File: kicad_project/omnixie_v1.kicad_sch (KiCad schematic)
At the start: 85 parts, among them J1 Conn_01x01, J2 Conn_01x04, J3 Conn_01x04, J4 USB_C_Receptacle_USB2.0_14P, Q0 Q_NMOS, Q1 Q_NMOS, Q10 Q_NMOS, Q100 Q_NMOS, Q11 Q_NMOS, Q2 Q_NMOS, Q3 Q_NMOS, Q4 Q_NMOS, Q5 Q_NMOS, Q6 Q_NMOS, Q7 Q_NMOS, Q8 Q_NMOS, Q9 Q_NMOS, T1 Flyback-ATB3225, U1 CH32V003F4U6, U2 4N25, U3 PI4IOE5V6416ZDEX

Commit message: component selection nearly done
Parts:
- removed D1: D, symbol Device:D
- removed H3, H4: MountingHole, MountingHole:MountingHole_2.7mm_M2.5_ISO7380_Pad_TopBottom, symbol MASTER_SYMBOLS:MountingHole_M2.5_RemoveWarning
- removed J1: Conn_01x01, symbol cnixxie:Conn_01x01
- removed N2, N3, N4, N5, N6: IN-1, NIXIE:IN-1_NIXIE_v1, symbol nixies-us:IN-1
- removed N9: IN-3, nixies-us:nixies-us-IN-3, symbol nixies-us:IN-3
- removed NX2, NX3, NX4, NX5, NX6: IN-12BORIGINAL, NIXIE:IN-12A Nixie, symbol nixies-us:IN-12BORIGINAL
- removed Q100: Q_NMOS, symbol Transistor_FET:Q_NMOS_GSD
- removed R10, R3, R5, R7, R? (x2): R, symbol cnixxie:R
- removed T1: Flyback-ATB3225, Flyback-ATB3225:Flyback-ATB3225, symbol cnixxie:Flyback-ATB3225
- removed TP1: VINPUT, symbol Connector:TestPoint
- removed TP2: VD, symbol Connector:TestPoint
- removed TP3: VOUTPUT, symbol Connector:TestPoint
- removed TP4: VFB, symbol Connector:TestPoint
- removed TP5: GATE, symbol Connector:TestPoint
- removed TP?: IOUTSENSE, symbol Connector:TestPoint
- removed TP?: IINSENSE, symbol Connector:TestPoint
- removed U2: 4N25, Package_DIP:DIP-6_W7.62mm, symbol Isolator:4N25
- added C3, C4, C5: 1uF, Capacitor_SMD:C_0805_2012Metric, symbol Device:C
- added FID5, FID6, FID7, FID8: Fiducial, Fiducial:Fiducial_0.5mm_Mask1mm, symbol MASTER_SYMBOLS:Fiducial
- added J1, J5: Conn_01x04, Connector_PinHeader_2.54mm:PinHeader_1x04_P2.54mm_Vertical, symbol Connector_Generic:Conn_01x04
- added J6, J7: Conn_01x02, Connector_PinHeader_2.54mm:PinHeader_1x02_P2.54mm_Vertical, symbol Connector_Generic:Conn_01x02
- C1: value C -> 10uF; footprint (none) -> Capacitor_SMD:C_0805_2012Metric
- C2: renamed from C?; value C -> 0.22uF; footprint (none) -> Capacitor_SMD:C_1210_3225Metric
- D2: renamed from D?; value D -> SK3200AFL-TP; footprint (none) -> OMNIXIE:SK3200AFL
- H1, H2: footprint MountingHole:MountingHole_2.7mm_M2.5_ISO7380_Pad_TopBottom -> MountingHole:MountingHole_2.2mm_M2_DIN965_Pad_TopOnly
- J2, J3: value Conn_01x04 -> SM04B-SRSS-TB
- J4: value USB_C_Receptacle_USB2.0_14P -> USB4105-GF-A
- N1, R1, R2: now not fitted; now left out of the parts list
- N2: renamed from NX1; now not fitted; now left out of the parts list
- N7, N8: value IN-3 -> IN-3/DOT; now not fitted; now left out of the parts list
- Q0, Q1, Q10, Q11, Q2, Q3, Q4, Q5, Q6, Q7, Q8, Q9: value Q_NMOS -> BSS123
- Q12: renamed from Q?; value Q_NMOS -> IPN50R1K4CEATMA1; footprint (none) -> Package_TO_SOT_SMD:SOT-223-3_TabPin2
- R11, R12: renamed from R?; value R -> 1k; footprint (none) -> Resistor_SMD:R_0805_2012Metric
- R13, R14: renamed from R?; footprint (none) -> Resistor_SMD:R_0603_1608Metric
- R15: renamed from R?; footprint (none) -> Resistor_SMD:R_0402_1005Metric_Pad0.72x0.64mm_HandSolder
- R3, R5: renamed from R?; value R -> 4.42m; footprint (none) -> Resistor_SMD:R_0402_1005Metric_Pad0.72x0.64mm_HandSolder
- R4: value R -> 82k; now not fitted; now left out of the parts list
- R6: value R -> 15k; footprint (none) -> Resistor_SMD:R_2010_5025Metric
- R7: renamed from R?; value R -> 100k; footprint (none) -> Resistor_SMD:R_0805_2012Metric
- R8, R9: value R -> 47; footprint (none) -> Resistor_SMD:R_0402_1005Metric_Pad0.72x0.64mm_HandSolder
- T2: renamed from T?; value Flyback-ATB3225 -> ATB322515-0110; footprint Flyback-ATB3225:Flyback-ATB3225 -> OMNIXIE:ATB322515
- TP10: renamed from TP?; value VINPUT -> 5005; footprint (none) -> TestPoint:TestPoint_Keystone_5005-5009_Compact
- TP11: renamed from TP?; value VD -> 5005; footprint (none) -> TestPoint:TestPoint_Keystone_5005-5009_Compact
- TP12: renamed from TP?; value VOUTPUT -> 5005; footprint (none) -> TestPoint:TestPoint_Keystone_5005-5009_Compact
- TP13: renamed from TP?; value VFB -> 5005; footprint (none) -> TestPoint:TestPoint_Keystone_5005-5009_Compact
- TP14: renamed from TP?; value GATE -> 5005; footprint (none) -> TestPoint:TestPoint_Keystone_5005-5009_Compact
- TP6: renamed from TP?; value IINSENSE -> 5005; footprint (none) -> TestPoint:TestPoint_Keystone_5005-5009_Compact
- TP8: renamed from TP?; value IOUTSENSE -> 5005; footprint (none) -> TestPoint:TestPoint_Keystone_5005-5009_Compact
- gave numbers to parts that had none: 1
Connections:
- net FEEDBACK is gone; now on net HV_FEEDBACK: R11.1, R7.2, TP13.1
- net INT_GATE is gone; now on net HV_SW: Q12.1 (G), R12.1, TP14.1
- net +3V3: now also C3.1, J1.3 (Pin_3), J5.3 (Pin_3)
- net +5V: now also C1.1, R3.2, TP10.1, C4.1, C5.1, J6.1 (Pin_1), J7.1 (Pin_1); no longer R3.1, T2.1, TP6.1
- net CATHAUX: now also N8.K
- net D+: now also R9.1; no longer U1.17 (PD3/A4/T2CH2/AETR/UCTS/T1CH4)
- net D-: now also R8.1; no longer R15.1, U1.18 (PD4/A7/UCK/T2CH1ETR/OPO/T1CH4ETR)
- net DPU: now also R15.1; no longer R15.2
- net GND: now also C3.2, C4.2, C5.2, J1.4 (Pin_4), J5.4 (Pin_4), J6.2 (Pin_2), J7.2 (Pin_2); no longer R9.2
- net HIGHVOLTAGE: now also R4.2; no longer R4.1, R5.1, R7.1, TP12.1
- net I2C_SCL: now also J1.2 (Pin_2), J5.2 (Pin_2)
- net I2C_SDA: now also J1.1 (Pin_1), J5.1 (Pin_1)
- net at N7.A: now also R4.1
- net at N7.K: now also N8.A
- net HV_FEEDBACK: now reaches U1.11 (PC4/A2/T1CH4/MCO/T1CH1CH2N)
- net HV_SW: now reaches U1.2 (PA1/OSCI/A1/T1CH2/OPN0)
- net at R6.2: now also R5.1, R7.1, TP12.1
- net at R8.2: now also R15.2, U1.18 (PD4/A7/UCK/T2CH1ETR/OPO/T1CH4ETR); no longer R9.1
- net IOUTSENSE: no longer names the net of C2.1, D2.1 (K), R5.2, TP8.1
- new net: R3.1, T2.1, TP6.1
- new net: R9.2, U1.17 (PD3/A4/T2CH2/AETR/UCTS/T1CH4)
- no-connect marks 0 -> 10
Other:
- note added: "+3V3 LDO"
- note added: "+5V Output"
- note added: "1:10 Turns Ratio"
- note added: "2 options for nixie hat connector"
- note added: "2.54mm Header Connections"
- note added: "Add PNs to BOM (saved in OneTab)"
- note added: "Compatibility for Driving the IN3s and the other small bulb looking ones"
- note added: "Figure out pinout for USB and analog inputs"
- note added: "Find small bulb sockets for the small nixie bulbs"
- note added: "Footprints for remaining components"
- note added: "For Driving Cathode MOSFETs"
- note added: "High Voltage! Flyback!"
- note added: "I/O Expander"
- note added: "I2C via..."
- note added: "It would be nice if the connector that connects the driver supply board to the nixie was reasonable to source"
- note added: "MOSFET Cathode Drivers"
- note added: "Maybe buy both and layout both connectors???"
- note added: "OMNIXIE"
- note added: "Output to Nixie Hat"
- note added: "QWIIC Compatible Connectors"
- note added: "Remaining passives values"
- note added: "Supply Input"
- note added: "The nixie driver supply board (Omnixie) would be awesome if all you had to do was either fab a super simple board or etch and homemake a nixie daughter board to use"
- note added: "To-Do"
- note added: "USB Compatibility"
- note added: "Vertical USB-C footprint"
- note added: "or"
- note removed: "Also I need to find a 200 V tolerant connector anyways if I'm going with the I2C GPIO approach anywas I require a connector that is at least 5 pins and relatively easy to take apart"
- note removed: "For control internally"
- note removed: "For dev and experimentation"
- note removed: "Unless I can find a relatively non-unicorn ~200V tolerant connector that has 12 pins, the mosfets will be on the nixie footprint board"
- company: (none) -> High Tech Aztech
- title: (none) -> Omnixie
- moved on the sheet: C2, D2, FID1, FID2, FID3, FID4, H1, H2, J2, J3, J4, Q0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

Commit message: component placement commencing
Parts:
- added J8: IL-WX-16S-VF-B-E1000E, OMNIXIE:IL-WX-16S-VF-B-E1000E-SOCKET, symbol Connector_Generic:Conn_02x08_Counter_Clockwise
- FID1, FID2, FID3, FID4, FID5, FID6, FID7, FID8: now not fitted
- H1, H2: footprint MountingHole:MountingHole_2.2mm_M2_DIN965_Pad_TopOnly -> MountingHole:MountingHole_2.2mm_M2
- J4: footprint Connector_USB:USB_C_Receptacle_Palconn_UTC16-G -> OMNIXIE:USB4120-03-C
- renumbered D2 to D1, T2 to T1
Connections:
- net CATH0: now also J8.1 (Pin_1)
- net CATH1: now also J8.2 (Pin_2)
- net CATH2: now also J8.3 (Pin_3)
- net CATH3: now also J8.4 (Pin_4)
- net CATH4: now also J8.5 (Pin_5)
- net CATH5: now also J8.6 (Pin_6)
- net CATH6: now also J8.7 (Pin_7)
- net CATH7: now also J8.8 (Pin_8)
- net CATH8: now also J8.9 (Pin_9)
- net CATH9: now also J8.10 (Pin_10)
- net CATHAUX: now also J8.12 (Pin_12)
- net CATHDP: now also J8.11 (Pin_11)
- net D+: now also R9.2, U1.17 (PD3/A4/T2CH2/AETR/UCTS/T1CH4)
- net D-: now also R15.2, R8.2, U1.18 (PD4/A7/UCK/T2CH1ETR/OPO/T1CH4ETR)
- net HIGHVOLTAGE: now also J8.15 (Pin_15), J8.16 (Pin_16)
- net at R3.1, T1.1, TP6.1: no longer names the net of R3.1, T1.1, TP6.1
- net HV_1: now reaches R5.1, R6.2, R7.1, TP12.1
- net D_2: now reaches C2.1, D1.1 (K), R5.2, TP8.1
- net D_1: now reaches D1.2 (A), T1.3, TP11.1
- net CC1: now reaches J4.A5 (CC1), R13.1
- net CC2: now reaches J4.B5 (CC2), R14.2
- no-connect marks 10 -> 12
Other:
- note added: "Done"
- note added: "Each board is individually programmed with the same program and communicate via I2C with each other to determine what each digit is"
- note added: "Idea"
- note added: "Next Revision?"
- note added: "PROGRAM pinout to edge?"
- note added: "Pinout of connector that could work well for routing nixie hat footprint"
- note added: "The connector that connects both boards should be reasonably sourceable"
- note added: "The nixie driver supply board will be separate from the nixie hat"
- note added: "change 1uf 1k and 100k to lower package size"
- note removed: "2 options for nixie hat connector"
- note removed: "It would be nice if the connector that connects the driver supply board to the nixie was reasonable to source"
- note removed: "Maybe buy both and layout both connectors???"
- note removed: "This means the power supplying must occur not on the nixie footprint board, but on the driver board"
- moved on the sheet: H1, H2, R13, R14

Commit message: more component placement
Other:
- note added: "Likely remove pinout on the right side of board"
- note added: "add diff pair to stackup, calculate width and spacing using calculator. standard FR4"
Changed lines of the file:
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@@
 		)
 	)
+	(text "add diff pair to stackup, calculate width and spacing using calculator. standard FR4"
+		(exclude_from_sim no)
+		(at 16.51 272.796 0)
+		(effects
+			(font
+				(size 1.27 1.27)
+				(thickness 0.3556)
+				(bold yes)
+				(italic yes)
+			)
+			(justify left)
+		)
+	)
 	(text "Vertical USB-C footprint\n"
 		(exclude_from_sim no)
@@
 		)
 	)
+	(text "Likely remove pinout on the right side of board"
+		(exclude_from_sim no)
+		(at 46.482 266.7 0)
+		(effects
+			(font
+				(size 1.27 1.27)
+				(thickness 0.3556)
+				(bold yes)
+				(italic yes)
+			)
+			(justify left)
+		)
+	)
 	(text "Output to Nixie Hat"
 		(exclude_from_sim no)
@@
 	(wire
 		(pts
-			(xy 63.5 152.4) (xy 66.04 152.4)
-		)
-		(stroke
-			(width 0)
-			(type default)
-		)
-	)
-	(wire
-		(pts
 			(xy 276.86 40.64) (xy 279.4 40.64)
 		)
@@
 	(symbol
 		(lib_id "power:+5V")
-		(at 63.5 152.4 0)
+		(at 66.04 152.4 0)
 		(unit 1)
 		(exclude_from_sim no)
@@
 		(dnp no)
 		(property "Reference" "#PWR033"
-			(at 63.5 156.21 0)
+			(at 66.04 156.21 0)
 			(effects
 				(font
@@
 		)
 		(property "Value" "+5V"
-			(at 62.992 147.828 0)
+			(at 65.532 147.828 0)
 			(effects
 				(font
@@
 		)
 		(property "Footprint" ""
-			(at 63.5 152.4 0)
+			(at 66.04 152.4 0)
 			(effects
 				(font
@@
 		)
 		(property "Datasheet" ""
-			(at 63.5 152.4 0)
+			(at 66.04 152.4 0)
 			(effects
 				(font
@@
 		)
 		(property "Description" "Power symbol creates a global label with name \"+5V\""
-			(at 63.5 152.4 0)
+			(at 66.04 152.4 0)
 			(effects
 				(font

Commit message: reworking the board. Its a prototype not production ready
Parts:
- removed H1, H2: MountingHole, MountingHole:MountingHole_2.2mm_M2, symbol MASTER_SYMBOLS:MountingHole_M2.5_RemoveWarning
- removed J1: Conn_01x04, Connector_PinHeader_2.54mm:PinHeader_1x04_P2.54mm_Vertical, symbol Connector_Generic:Conn_01x04
- removed J7: Conn_01x02, Connector_PinHeader_2.54mm:PinHeader_1x02_P2.54mm_Vertical, symbol Connector_Generic:Conn_01x02
- added D2, D8: GREEN, LED_SMD:LED_0603_1608Metric, symbol MASTER_SYMBOLS:LED_Small
- added FID10, FID11, FID12, FID13, FID14, FID15, FID9: Fiducial, Fiducial:Fiducial_0.5mm_Mask1mm, symbol MASTER_SYMBOLS:Fiducial
- added J1: Conn_01x10, Connector_PinHeader_2.54mm:PinHeader_1x10_P2.54mm_Vertical, symbol Connector_Generic:Conn_01x10
- added JP10: Jumper_2_Bridged, MASTER_FOOTPRINTS:SolderJumper_Rect_0.2mm_spacing, symbol Jumper:Jumper_2_Bridged
- added JP11: Jumper_2_Bridged, MASTER_FOOTPRINTS:SolderJumper_Circular_0.2mm_spacing, symbol Jumper:Jumper_2_Bridged
- added JP12: Jumper_2_Bridged, MASTER_FOOTPRINTS:SolderJumper_Circular_0.1mm_spacing, symbol Jumper:Jumper_2_Bridged
- added JP13: Jumper_2_Bridged, MASTER_FOOTPRINTS:SolderJumper_PinHeader_0.1mm_spacing, symbol Jumper:Jumper_2_Bridged
- added JP14: Jumper_2_Bridged, MASTER_FOOTPRINTS:SolderJumper_Circular_0.05mm_spacing, symbol Jumper:Jumper_2_Bridged
- added JP4: SMT_THERM_JMP, Jumper:SolderJumper-2_P1.3mm_Bridged_RoundedPad1.0x1.5mm, symbol MASTER_SYMBOLS:SolderJumper_2_Bridged_4
- added JP5: TH_THERM_JMP, Jumper:SolderJumper-2_P1.3mm_Open_RoundedPad1.0x1.5mm, symbol MASTER_SYMBOLS:SolderJumper_2_Open
- added JP7: Jumper_2_Bridged, MASTER_FOOTPRINTS:SolderJumper_Rect_0.3mm_spacing, symbol Jumper:Jumper_2_Bridged
- added R10, R16: 10k, Resistor_SMD:R_0402_1005Metric, symbol MASTER_SYMBOLS:R_Small_17
- C3, C4, C5: footprint Capacitor_SMD:C_0805_2012Metric -> Capacitor_SMD:C_0603_1608Metric
- J6: footprint Connector_PinHeader_2.54mm:PinHeader_1x02_P2.54mm_Vertical -> Connector_PinHeader_2.54mm:PinHeader_1x03_P2.54mm_Vertical; symbol Connector_Generic:Conn_01x02 -> Connector_Generic:Conn_01x03
- R11, R12: footprint Resistor_SMD:R_0805_2012Metric -> Resistor_SMD:R_0603_1608Metric
- R3, R5: value 4.42m -> 10m; footprint Resistor_SMD:R_0402_1005Metric_Pad0.72x0.64mm_HandSolder -> Resistor_SMD:R_0603_1608Metric
- R7: footprint Resistor_SMD:R_0805_2012Metric -> Resistor_SMD:R_0402_1005Metric_Pad0.72x0.64mm_HandSolder
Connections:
- net +3V3: now also D8.2 (A), JP4.1 (A); no longer U3.21 (VDD_P), U3.23 (VDD_I2C)
- net +5V: now also D2.2 (A), JP5.1 (A); no longer C5.1, R3.2, T1.2, TP10.1
- net D+: no longer R9.2, U1.17 (PD3/A4/T2CH2/AETR/UCTS/T1CH4)
- net D-: no longer R15.2, R8.2, U1.18 (PD4/A7/UCK/T2CH1ETR/OPO/T1CH4ETR)
- net DIG_0: now also U3.2 (IO0_1); no longer U3.1 (IO0_0)
- net DIG_1: now also U3.1 (IO0_0); no longer U3.2 (IO0_1)
- net DIG_2: now also U3.4 (IO0_3); no longer U3.3 (IO0_2)
- net DIG_3: now also U3.3 (IO0_2); no longer U3.4 (IO0_3)
- net DIG_4: now also U3.6 (IO0_5); no longer U3.5 (IO0_4)
- net DIG_5: now also U3.5 (IO0_4); no longer U3.6 (IO0_5)
- net DIG_6: now also U3.8 (IO0_7); no longer U3.7 (IO0_6)
- net DIG_7: now also U3.7 (IO0_6); no longer U3.8 (IO0_7)
- net DIG_8: now also U3.11 (IO1_1); no longer U3.10 (IO1_0)
- net DIG_9: now also U3.10 (IO1_0); no longer U3.11 (IO1_1)
- net DIG_AUX: now also U3.12 (IO1_2); no longer U3.13 (IO1_3)
- net DIG_DP: now also U3.13 (IO1_3); no longer U3.12 (IO1_2)
- net GND: now also R10.1, R16.1
- net HV_SW: now also U1.14 (PC7/MISO/T1CH2/T2CH2/URTS); no longer U1.2 (PA1/OSCI/A1/T1CH2/OPN0)
- net I2C_SCL: now also J5.1 (Pin_1); no longer J5.2 (Pin_2)
- net I2C_SDA: now also J5.2 (Pin_2); no longer J5.1 (Pin_1)
- net PROGRAM: now also J6.3 (Pin_3)
- net PD7: now reaches U1.1 (PD7/NRST/T2CH4/OPP1/UCK)
- net PD7: now also J1.9 (Pin_9)
- net PC5: now reaches U1.12 (PC5/SCK/T1ETR/T2CH1ETR/SCL/UCK/T1CH3)
- net PC5: now also J1.3 (Pin_3)
- net PC6: now reaches U1.13 (PC6/MOSI/T1CH1CH3/UCTS/SDA)
- net PC6: now also J1.2 (Pin_2)
- net PD2: now reaches U1.16 (PD2/A3/T1CH1/T2CH3/T1CH2N)
- net PD2: now also J1.1 (Pin_1)
- net PD6: now reaches U1.20 (PD6/A7/URX/T2CH3/UTX)
- net PD6: now also J1.10 (Pin_10)
- net PA2: now reaches U1.3 (PA2/OSCO/A0/T1CH2N/OPP0/AETR2)
- net PA2: now also J1.7 (Pin_7)
- net PD0: now reaches U1.5 (PD0/T1CH1N/OPN1/SDA/UTX)
- net PD0: now also J1.6 (Pin_6)
- net PC0: now reaches U1.7 (PC0/T2CH3/UTX/NSS/T1CH3)
- net PC0: now also J1.5 (Pin_5)
- net PC1: now reaches U1.8 (PC1/SDA/NSS/T2CH4/T2CH1ETR/T1BKIN/URX)
- net PC1: now also J1.4 (Pin_4)
- new net: JP4.2 (B), U3.21 (VDD_P), U3.23 (VDD_I2C)
- new net: D2.1 (K), R16.2
- new net: D8.1 (K), R10.2
- new net +5V_FLY: C5.1, JP5.2 (B), R3.2, T1.2, TP10.1
- new net D+_1: R9.2, U1.17 (PD3/A4/T2CH2/AETR/UCTS/T1CH4)
- new net D-_1: R15.2, R8.2, U1.18 (PD4/A7/UCK/T2CH1ETR/OPO/T1CH4ETR)
- new net PA1: J1.8 (Pin_8), U1.2 (PA1/OSCI/A1/T1CH2/OPN0)
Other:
- note added: "+5V Output w/ Programming SWD"
- note added: "POWER INDICATOR LEDS"
- note added: "REMAINING MCU BREAKOUT"
- note added: "USB-C INPUT"
- note removed: "+5V Output"
- note removed: "Supply Input"
- title: Omnixie -> Omnixie PROTOTYPE
- moved on the sheet: C4, J5, R15, R8, R9, TP13, U1

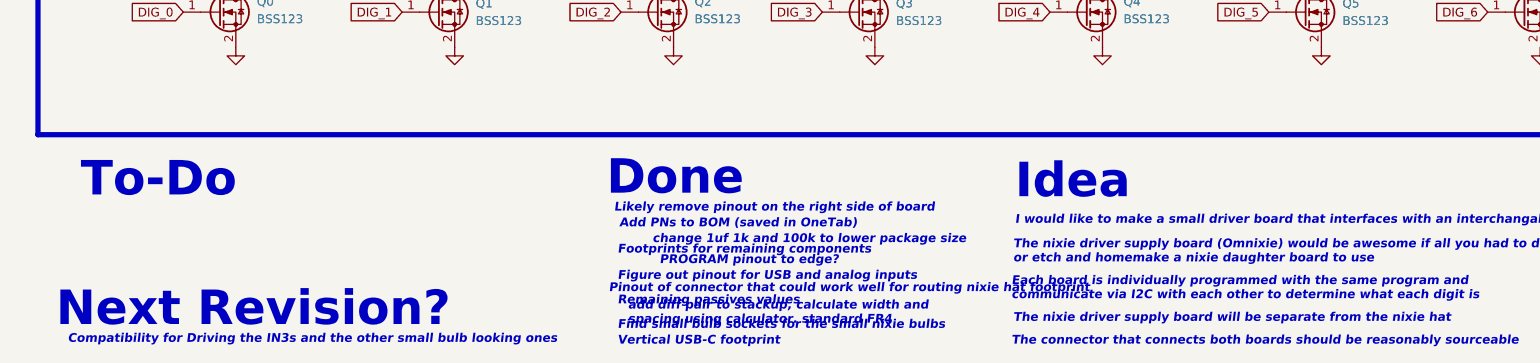
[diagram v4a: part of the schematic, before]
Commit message: new component placement pretty much done
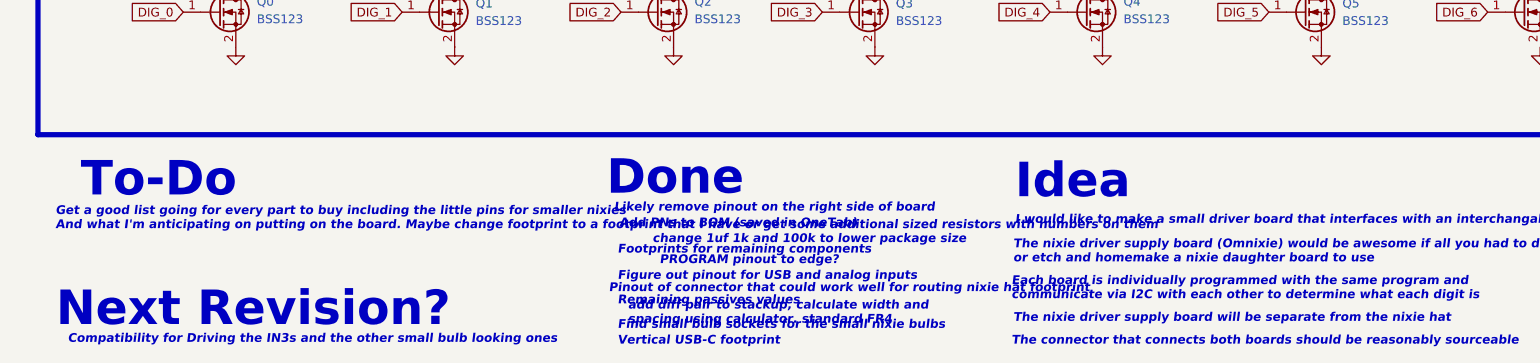
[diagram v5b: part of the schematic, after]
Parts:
- J2, J3: now left out of the parts list
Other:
- note added: "Get a good list going for every part to buy including the little pins for smaller nixies And what I'm anticipating on putting on the board. Maybe change footprint to a footprint that I have or get some additional sized resistors with numbers on them"

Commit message: home from christmas in vegas
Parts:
- renumbered D8 to D3
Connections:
- net +3V3: now also C4.1, U1.6 (VDD)
- net +5V: no longer C4.1, U1.6 (VDD)
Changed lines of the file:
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@@
 	(text "Get a good list going for every part to buy including the little pins for smaller nixies\nAnd what I'm anticipating on putting on the board. Maybe change footprint to a footprint that I have or get some additional sized resistors with numbers on them"
 		(exclude_from_sim no)
-		(at 14.478 264.922 0)
+		(at 15.24 267.462 0)
 		(effects
 			(font
@@
 	)
 	(symbol
-		(lib_id "power:+5V")
-		(at 99.06 55.88 0)
-		(unit 1)
-		(exclude_from_sim no)
-		(in_bom yes)
-		(on_board yes)
-		(dnp no)
-		(property "Reference" "#PWR017"
-			(at 99.06 59.69 0)
-			(effects
-				(font
-					(size 1.27 1.27)
-				)
-				(hide yes)
-			)
-		)
-		(property "Value" "+5V"
-			(at 99.06 52.07 0)
-			(effects
-				(font
-					(size 1.27 1.27)
-				)
-			)
-		)
-		(property "Footprint" ""
-			(at 99.06 55.88 0)
-			(effects
-				(font
-					(size 1.27 1.27)
-				)
-				(hide yes)
-			)
-		)
-		(property "Datasheet" ""
-			(at 99.06 55.88 0)
-			(effects
-				(font
-					(size 1.27 1.27)
-				)
-				(hide yes)
-			)
-		)
-		(property "Description" "Power symbol creates a global label with name \"+5V\""
-			(at 99.06 55.88 0)
-			(effects
-				(font
-					(size 1.27 1.27)
-				)
-				(hide yes)
-			)
-		)
-		(pin "1"
-		)
-		(instances
-			(project "omnixie_v1"
-				(path "/7791313b-9c26-4810-8a43-0e3a20909b33"
-					(reference "#PWR017")
-					(unit 1)
-				)
-			)
-		)
-	)
-	(symbol
 		(lib_id "cnixxie:Flyback-ATB3225")
 		(at 100.33 160.02 270)
@@
 	)
 	(symbol
+		(lib_id "power:+5V")
+		(at 99.06 55.88 0)
+		(unit 1)
+		(exclude_from_sim no)
+		(in_bom yes)
+		(on_board yes)
+		(dnp no)
+		(property "Reference" "#PWR017"
+			(at 99.06 59.69 0)
+			(effects
+				(font
+					(size 1.27 1.27)
+				)
+				(hide yes)
+			)
+		)
+		(property "Value" "+3V3"
+			(at 98.806 52.07 0)
+			(effects
+				(font
+					(size 1.27 1.27)
+				)
+			)
+		)
+		(property "Footprint" ""
+			(at 99.06 55.88 0)
+			(effects
+				(font
+					(size 1.27 1.27)
+				)
+				(hide yes)
+			)
+		)
+		(property "Datasheet" ""
+			(at 99.06 55.88 0)
+			(effects
+				(font
+					(size 1.27 1.27)
+				)
+				(hide yes)
+			)
+		)
+		(property "Description" "Power symbol creates a global label with name \"+5V\""
+			(at 99.06 55.88 0)
+			(effects
+				(font
+					(size 1.27 1.27)
+				)
+				(hide yes)
+			)
+		)
+		(pin "1"
+		)
+		(instances
+			(project "omnixie_v1"
+				(path "/7791313b-9c26-4810-8a43-0e3a20909b33"
+					(reference "#PWR017")
+					(unit 1)
+				)
+			)
+		)
+	)
+	(symbol
 		(lib_id "MASTER_SYMBOLS:Fiducial")
 		(at 444.5 212.09 0)
@@
 		(on_board yes)
 		(dnp no)
-		(property "Reference" "D8"
+		(property "Reference" "D3"
 			(at 118.11 95.1864 90)
 			(effects
@@
 			(project "omnixie_v1"
 				(path "/7791313b-9c26-4810-8a43-0e3a20909b33"
-					(reference "D8")
+					(reference "D3")
 					(unit 1)
 				)
